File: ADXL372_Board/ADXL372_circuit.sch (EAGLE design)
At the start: 38 parts, among them IC4 SI7006-A20-IM, IC5 LP5907MFX-2.5/NOPB, Q2 BSS138W, SW1 DHT-4235A, U1 MX25R1635FM1IL0, U2 ADXL345BCCZ, U3 ADXL372BCCZ-RL7, Y1 16MHZ_X053201602002, Y2 3.2768KHZ

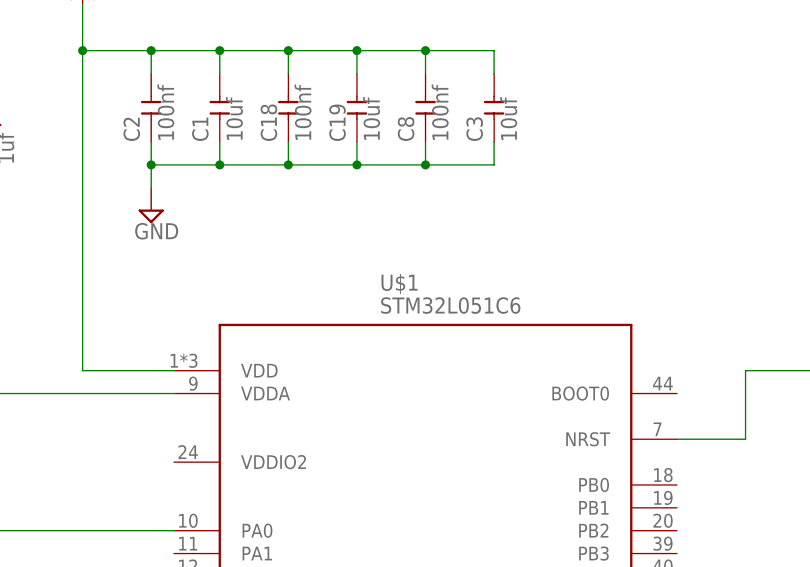
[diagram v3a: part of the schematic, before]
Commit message: パターン図を修正
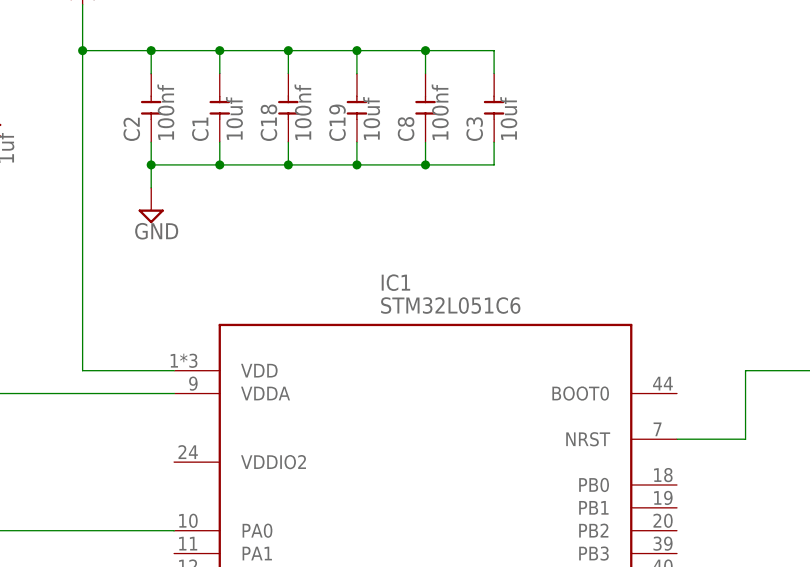
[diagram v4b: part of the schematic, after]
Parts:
- renumbered U$1 to IC1
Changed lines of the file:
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@@
 <part name="SUPPLY21" library="supply2" library_urn="urn:adsk.eagle:library:372" deviceset="GND" device=""/>
 <part name="Y1" library="OPL_Crystal Oscillator" library_urn="urn:adsk.eagle:library:8004402" deviceset="SMD-CRYSTAL-16MHZ-8PF-20PPM-40R(2P-5.0X3.2MM)" device="" package3d_urn="urn:adsk.eagle:package:8004459/1" value="16MHZ_X053201602002"/>
-<part name="U$1" library="stm32l05x6" library_urn="urn:adsk.eagle:library:14260580" deviceset="STM32L051C6" device="" package3d_urn="urn:adsk.eagle:package:19290/2"/>
+<part name="IC1" library="stm32l05x6" library_urn="urn:adsk.eagle:library:14260580" deviceset="STM32L051C6" device="" package3d_urn="urn:adsk.eagle:package:19290/2"/>
 <part name="C18" library="OPL_Capacitor" deviceset="CERAMIC-100NF-50V-10%-X7R(0603)" device="" package3d_urn="urn:adsk.eagle:package:8004287/1" value="100nf"/>
 <part name="C19" library="OPL_Capacitor" deviceset="CERAMIC-10UF-10V-(-20%～+80%)-Y5V(0805)" device="" package3d_urn="urn:adsk.eagle:package:8004286/1" value="10uf"/>
@@
 <attribute name="VALUE" x="138.43" y="96.52" size="1.27" layer="96" ratio="10"/>
 </instance>
-<instance part="U$1" gate="G$1" x="185.42" y="142.24" smashed="yes">
+<instance part="IC1" gate="G$1" x="185.42" y="142.24" smashed="yes">
 <attribute name="NAME" x="180.34" y="186.69" size="1.778" layer="95"/>
 <attribute name="VALUE" x="180.34" y="184.15" size="1.778" layer="96"/>
@@
 <wire x1="177.8" y1="210.82" x2="177.8" y2="213.36" width="0.1524" layer="91"/>
 <junction x="177.8" y="213.36"/>
-<pinref part="U$1" gate="G$1" pin="VDD"/>
+<pinref part="IC1" gate="G$1" pin="VDD"/>
 <wire x1="157.48" y1="177.8" x2="147.32" y2="177.8" width="0.1524" layer="91"/>
 </segment>
@@
 <pinref part="C12" gate="G$1" pin="2"/>
 <pinref part="VCC2" gate="G$1" pin="+3V3"/>
-<pinref part="U$1" gate="G$1" pin="VDDA"/>
+<pinref part="IC1" gate="G$1" pin="VDDA"/>
 <wire x1="157.48" y1="175.26" x2="121.92" y2="175.26" width="0.1524" layer="91"/>
 </segment>
@@
 <pinref part="SUPPLY2" gate="GND" pin="GND"/>
 <wire x1="218.44" y1="101.6" x2="218.44" y2="95.25" width="0.1524" layer="91"/>
-<pinref part="U$1" gate="G$1" pin="VSS"/>
+<pinref part="IC1" gate="G$1" pin="VSS"/>
 <wire x1="213.36" y1="101.6" x2="218.44" y2="101.6" width="0.1524" layer="91"/>
 </segment>
@@
 <wire x1="144.78" y1="109.22" x2="139.7" y2="109.22" width="0.1524" layer="91"/>
 <wire x1="144.78" y1="107.95" x2="144.78" y2="109.22" width="0.1524" layer="91"/>
-<pinref part="U$1" gate="G$1" pin="PC14-OSC32_IN"/>
+<pinref part="IC1" gate="G$1" pin="PC14-OSC32_IN"/>
 <wire x1="157.48" y1="109.22" x2="144.78" y2="109.22" width="0.1524" layer="91"/>
 <junction x="144.78" y="109.22"/>
@@
 <wire x1="144.78" y1="99.06" x2="144.78" y2="100.33" width="0.1524" layer="91"/>
 <junction x="144.78" y="99.06"/>
-<pinref part="U$1" gate="G$1" pin="PC15-OSC32_OUT"/>
+<pinref part="IC1" gate="G$1" pin="PC15-OSC32_OUT"/>
 <wire x1="157.48" y1="104.14" x2="149.86" y2="104.14" width="0.1524" layer="91"/>
 </segment>
@@
 <wire x1="243.84" y1="175.26" x2="243.84" y2="177.8" width="0.1524" layer="91"/>
 <junction x="243.84" y="177.8"/>
-<pinref part="U$1" gate="G$1" pin="NRST"/>
+<pinref part="IC1" gate="G$1" pin="NRST"/>
 <wire x1="213.36" y1="170.18" x2="220.98" y2="170.18" width="0.1524" layer="91"/>
 <wire x1="220.98" y1="170.18" x2="220.98" y2="177.8" width="0.1524" layer="91"/>
@@
 <label x="55.88" y="33.02" size="1.778" layer="95"/>
 <label x="193.04" y="45.72" size="1.778" layer="95"/>
-<pinref part="U$1" gate="G$1" pin="PA5"/>
+<pinref part="IC1" gate="G$1" pin="PA5"/>
 </segment>
 <segment>
@@
 <label x="193.04" y="38.1" size="1.778" layer="95"/>
 <label x="144.78" y="45.72" size="1.778" layer="95"/>
-<pinref part="U$1" gate="G$1" pin="PA6"/>
+<pinref part="IC1" gate="G$1" pin="PA6"/>
 </segment>
 <segment>
@@
 <label x="193.04" y="40.64" size="1.778" layer="95"/>
 <label x="144.78" y="50.8" size="1.778" layer="95"/>
-<pinref part="U$1" gate="G$1" pin="PA7"/>
+<pinref part="IC1" gate="G$1" pin="PA7"/>
 </segment>
 <segment>
@@
 <label x="132.08" y="139.7" size="1.778" layer="95"/>
 <label x="55.88" y="38.1" size="1.778" layer="95"/>
-<pinref part="U$1" gate="G$1" pin="PA8"/>
+<pinref part="IC1" gate="G$1" pin="PA8"/>
 </segment>
 </net>
@@
 <label x="132.08" y="137.16" size="1.778" layer="95"/>
 <label x="193.04" y="43.18" size="1.778" layer="95"/>
-<pinref part="U$1" gate="G$1" pin="PA9"/>
+<pinref part="IC1" gate="G$1" pin="PA9"/>
 </segment>
 </net>
@@
 <wire x1="157.48" y1="134.62" x2="129.54" y2="134.62" width="0.1524" layer="91"/>
 <label x="132.08" y="134.62" size="1.778" layer="95"/>
-<pinref part="U$1" gate="G$1" pin="PA10"/>
+<pinref part="IC1" gate="G$1" pin="PA10"/>
 </segment>
 </net>
@@
 <net name="I2C1_SCL" class="0">
 <segment>
-<pinref part="U$1" gate="G$1" pin="PB8"/>
+<pinref part="IC1" gate="G$1" pin="PB8"/>
 <wire x1="213.36" y1="144.78" x2="238.76" y2="144.78" width="0.1524" layer="91"/>
 <label x="220.98" y="144.78" size="1.778" layer="95"/>
@@
 <net name="I2C1_SDA" class="0">
 <segment>
-<pinref part="U$1" gate="G$1" pin="PB9"/>
+<pinref part="IC1" gate="G$1" pin="PB9"/>
 <wire x1="213.36" y1="142.24" x2="238.76" y2="142.24" width="0.1524" layer="91"/>
 <label x="220.98" y="142.24" size="1.778" layer="95"/>
@@
 <net name="I2C2_SCL" class="0">
 <segment>
-<pinref part="U$1" gate="G$1" pin="PB13"/>
+<pinref part="IC1" gate="G$1" pin="PB13"/>
 <wire x1="213.36" y1="132.08" x2="238.76" y2="132.08" width="0.1524" layer="91"/>
 <label x="220.98" y="132.08" size="1.778" layer="95"/>
@@
 <net name="I2C2_SDA" class="0">
 <segment>
-<pinref part="U$1" gate="G$1" pin="PB14"/>
+<pinref part="IC1" gate="G$1" pin="PB14"/>
 <wire x1="213.36" y1="129.54" x2="238.76" y2="129.54" width="0.1524" layer="91"/>
 <label x="220.98" y="129.54" size="1.778" layer="95"/>
@@
 <net name="N$14" class="0">
 <segment>
-<pinref part="U$1" gate="G$1" pin="PH0-OSC_IN"/>
+<pinref part="IC1" gate="G$1" pin="PH0-OSC_IN"/>
 <wire x1="213.36" y1="119.38" x2="233.68" y2="119.38" width="0.1524" layer="91"/>
 <pinref part="Y2" gate="G$1" pin="2"/>
@@
 <net name="N$15" class="0">
 <segment>
-<pinref part="U$1" gate="G$1" pin="PH1-OSC_OUT"/>
+<pinref part="IC1" gate="G$1" pin="PH1-OSC_OUT"/>
 <wire x1="213.36" y1="114.3" x2="223.52" y2="114.3" width="0.1524" layer="91"/>
 <wire x1="223.52" y1="114.3" x2="223.52" y2="106.68" width="0.1524" layer="91"/>
@@
 <net name="N$17" class="0">
 <segment>
-<pinref part="U$1" gate="G$1" pin="PA0"/>
+<pinref part="IC1" gate="G$1" pin="PA0"/>
 <wire x1="157.48" y1="160.02" x2="114.3" y2="160.02" width="0.1524" layer="91"/>
 <wire x1="114.3" y1="160.02" x2="114.3" y2="139.7" width="0.1524" layer="91"/>

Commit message: 回路図修正
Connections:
- removed net N$16: IC1.PA10
- removed net N$24: U1.CS#
- removed net N$5: U3.SCLK
- removed net N$6: U3.!CS!/SCL
- removed net N$7: U3.MOSI/SDA
- removed net N$8: U3.MISO
- new net FLASH_MEMORY: IC1.PA10, U1.CS#
- net ADXL372_CS: now also U3.!CS!/SCL
- net SPI1_MISO: now also U3.MISO
- net SPI1_MOSI: now also U3.MOSI/SDA
- net SPI1_SCK: now also U3.SCLK
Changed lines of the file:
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@@
 <part name="BT1" library="BU2032SM-HD-G" library_urn="urn:adsk.eagle:library:14268586" deviceset="BU2032SM-HD-G" device="" package3d_urn="urn:adsk.eagle:package:14268589/1"/>
 <part name="VCC1" library="supply1" library_urn="urn:adsk.eagle:library:371" deviceset="+3V3" device="" value="+2V5"/>
-<part name="VCC2" library="supply1" library_urn="urn:adsk.eagle:library:371" deviceset="+3V3" device="" value="+2V5"/>
+<part name="VCC" library="supply1" library_urn="urn:adsk.eagle:library:371" deviceset="+3V3" device="" value="+2V5"/>
 <part name="VCC3" library="supply1" library_urn="urn:adsk.eagle:library:371" deviceset="+3V3" device="" value="+2V5"/>
 <part name="VCC4" library="supply1" library_urn="urn:adsk.eagle:library:371" deviceset="+3V3" device="" value="+2V5"/>
@@
 <attribute name="VALUE" x="144.78" y="222.25" size="1.778" layer="96"/>
 </instance>
-<instance part="VCC2" gate="G$1" x="121.92" y="218.44" smashed="yes">
+<instance part="VCC" gate="G$1" x="121.92" y="218.44" smashed="yes">
 <attribute name="VALUE" x="119.38" y="219.71" size="1.778" layer="96"/>
 </instance>
@@
 <pinref part="C11" gate="G$1" pin="2"/>
 <pinref part="C12" gate="G$1" pin="2"/>
-<pinref part="VCC2" gate="G$1" pin="+3V3"/>
+<pinref part="VCC" gate="G$1" pin="+3V3"/>
 <pinref part="IC1" gate="G$1" pin="VDDA"/>
 <wire x1="157.48" y1="175.26" x2="121.92" y2="175.26" width="0.1524" layer="91"/>
@@
 <label x="132.08" y="147.32" size="1.778" layer="95"/>
 <label x="55.88" y="33.02" size="1.778" layer="95"/>
-<label x="193.04" y="45.72" size="1.778" layer="95"/>
 <pinref part="IC1" gate="G$1" pin="PA5"/>
 </segment>
@@
 <label x="289.56" y="119.38" size="1.778" layer="95"/>
 </segment>
+<segment>
+<pinref part="U3" gate="G$1" pin="SCLK"/>
+<wire x1="210.82" y1="45.72" x2="190.5" y2="45.72" width="0.1524" layer="91"/>
+<label x="193.04" y="45.72" size="1.778" layer="95"/>
+</segment>
 </net>
 <net name="SPI1_MISO" class="0">
@@
 <wire x1="157.48" y1="144.78" x2="129.54" y2="144.78" width="0.1524" layer="91"/>
 <label x="132.08" y="144.78" size="1.778" layer="95"/>
-<label x="193.04" y="38.1" size="1.778" layer="95"/>
-<label x="193.04" y="38.1" size="1.778" layer="95"/>
 <label x="144.78" y="45.72" size="1.778" layer="95"/>
 <pinref part="IC1" gate="G$1" pin="PA6"/>
@@
 <label x="289.56" y="114.3" size="1.778" layer="95"/>
 </segment>
+<segment>
+<pinref part="U3" gate="G$1" pin="MISO"/>
+<wire x1="210.82" y1="38.1" x2="190.5" y2="38.1" width="0.1524" layer="91"/>
+<label x="193.04" y="38.1" size="1.778" layer="95"/>
+</segment>
 </net>
 <net name="SPI1_MOSI" class="0">
@@
 <wire x1="157.48" y1="142.24" x2="129.54" y2="142.24" width="0.1524" layer="91"/>
 <label x="132.08" y="142.24" size="1.778" layer="95"/>
-<label x="193.04" y="40.64" size="1.778" layer="95"/>
 <label x="144.78" y="50.8" size="1.778" layer="95"/>
 <pinref part="IC1" gate="G$1" pin="PA7"/>
@@
 <label x="289.56" y="116.84" size="1.778" layer="95"/>
 </segment>
+<segment>
+<pinref part="U3" gate="G$1" pin="MOSI/SDA"/>
+<wire x1="210.82" y1="40.64" x2="190.5" y2="40.64" width="0.1524" layer="91"/>
+<label x="193.04" y="40.64" size="1.778" layer="95"/>
+</segment>
 </net>
 <net name="N$4" class="0">
@@
 <pinref part="U2" gate="A" pin="SCL/SCLK"/>
 <wire x1="53.34" y1="33.02" x2="76.2" y2="33.02" width="0.1524" layer="91"/>
-</segment>
-</net>
-<net name="N$5" class="0">
-<segment>
-<pinref part="U3" gate="G$1" pin="SCLK"/>
-<wire x1="210.82" y1="45.72" x2="190.5" y2="45.72" width="0.1524" layer="91"/>
-</segment>
-</net>
-<net name="N$6" class="0">
-<segment>
-<pinref part="U3" gate="G$1" pin="!CS!/SCL"/>
-<wire x1="210.82" y1="43.18" x2="190.5" y2="43.18" width="0.1524" layer="91"/>
-</segment>
-</net>
-<net name="N$7" class="0">
-<segment>
-<pinref part="U3" gate="G$1" pin="MOSI/SDA"/>
-<wire x1="210.82" y1="40.64" x2="190.5" y2="40.64" width="0.1524" layer="91"/>
-</segment>
-</net>
-<net name="N$8" class="0">
-<segment>
-<pinref part="U3" gate="G$1" pin="MISO"/>
-<wire x1="210.82" y1="38.1" x2="190.5" y2="38.1" width="0.1524" layer="91"/>
 </segment>
 </net>
@@
 <wire x1="157.48" y1="137.16" x2="129.54" y2="137.16" width="0.1524" layer="91"/>
 <label x="132.08" y="137.16" size="1.778" layer="95"/>
+<pinref part="IC1" gate="G$1" pin="PA9"/>
+</segment>
+<segment>
+<pinref part="U3" gate="G$1" pin="!CS!/SCL"/>
+<wire x1="210.82" y1="43.18" x2="190.5" y2="43.18" width="0.1524" layer="91"/>
 <label x="193.04" y="43.18" size="1.778" layer="95"/>
-<pinref part="IC1" gate="G$1" pin="PA9"/>
-</segment>
-</net>
-<net name="N$16" class="0">
-<segment>
-<wire x1="157.48" y1="134.62" x2="129.54" y2="134.62" width="0.1524" layer="91"/>
-<label x="132.08" y="134.62" size="1.778" layer="95"/>
-<pinref part="IC1" gate="G$1" pin="PA10"/>
 </segment>
 </net>
@@
 </segment>
 </net>
-<net name="N$24" class="0">
+<net name="FLASH_MEMORY" class="0">
 <segment>
 <pinref part="U1" gate="G$1" pin="CS#"/>
 <wire x1="309.88" y1="121.92" x2="287.02" y2="121.92" width="0.1524" layer="91"/>
+<label x="289.56" y="121.92" size="1.778" layer="95"/>
+</segment>
+<segment>
+<wire x1="157.48" y1="134.62" x2="129.54" y2="134.62" width="0.1524" layer="91"/>
+<label x="132.08" y="134.62" size="1.778" layer="95"/>
+<pinref part="IC1" gate="G$1" pin="PA10"/>
 </segment>
 </net>
@@
 </segment>
 </net>
-<net name="VCC" class="0">
-<segment>
-<pinref part="+2V5" gate="VCC" pin="VCC"/>
-<pinref part="C15" gate="G$1" pin="2"/>
-<wire x1="93.98" y1="238.76" x2="93.98" y2="233.68" width="0.1524" layer="91"/>
-<pinref part="IC5" gate="G$1" pin="OUT"/>
-<wire x1="93.98" y1="233.68" x2="93.98" y2="231.14" width="0.1524" layer="91"/>
-<wire x1="71.12" y1="233.68" x2="86.36" y2="233.68" width="0.1524" layer="91"/>
-<junction x="93.98" y="233.68"/>
-<pinref part="C7" gate="G$1" pin="2"/>
-<wire x1="86.36" y1="233.68" x2="93.98" y2="233.68" width="0.1524" layer="91"/>
-<wire x1="86.36" y1="231.14" x2="86.36" y2="233.68" width="0.1524" layer="91"/>
-<junction x="86.36" y="233.68"/>
-</segment>
-</net>
 <net name="N$17" class="0">
 <segment>
@@
 </segment>
 </net>
+<net name="VCC" class="0">
+<segment>
+<pinref part="C7" gate="G$1" pin="2"/>
+<wire x1="86.36" y1="231.14" x2="86.36" y2="233.68" width="0.1524" layer="91"/>
+<pinref part="IC5" gate="G$1" pin="OUT"/>
+<wire x1="71.12" y1="233.68" x2="86.36" y2="233.68" width="0.1524" layer="91"/>
+<wire x1="86.36" y1="233.68" x2="93.98" y2="233.68" width="0.1524" layer="91"/>
+<junction x="86.36" y="233.68"/>
+<pinref part="+2V5" gate="VCC" pin="VCC"/>
+<wire x1="93.98" y1="238.76" x2="93.98" y2="233.68" width="0.1524" layer="91"/>
+<pinref part="C15" gate="G$1" pin="2"/>
+<wire x1="93.98" y1="231.14" x2="93.98" y2="233.68" width="0.1524" layer="91"/>
+<junction x="93.98" y="233.68"/>
+</segment>
+</net>

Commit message: Update circuit
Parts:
- removed U1: MX25R1635FM1IL0, MX25R1635FM1IL0:MX25R1635FM1IL0
- removed U2: ADXL345BCCZ, ADXL345BCCZ:ADXL345BCCZ
- removed U3: ADXL372BCCZ-RL7, ADXL372BCCZ-RL7:ADXL372BCCZ-RL7
- added CN1: FH12-08S-1SH, con-hirose:FH12-08S-1SH
- added IC2: ADXL345BCCZ, ADXL345BCCZ:ADXL345BCCZ
- added IC3: ADXL372BCCZ-RL7, ADXL372BCCZ-RL7:ADXL372BCCZ-RL7
- added IC6: MX25R1635FM1IL0, MX25R1635FM1IL0:MX25R1635FM1IL0
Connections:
- removed net N$10: U2.SDA/SDI/SDIO
- removed net N$11: U2.SDO/ALT_ADDRESS
- removed net N$17: IC1.PA0, R5.2
- removed net N$20: Q2.G, R4.2, R5.1
- removed net N$9: U2.*CS
- new net SPI1_NSS: IC1.PA4
- new net SPI2_MISO: IC1.PB14, IC6.SO/SIO1
- new net SPI2_MOSI: IC1.PB15, IC6.SI/SIO0
- new net SPI2_NSS: IC1.PB12
- new net SPI2_SCK: IC1.PB13, IC6.SCLK
- new net USART1_CK: CN1-3.1, IC1.PA8
- new net USART1_RX: CN1-5.1, IC1.PA10
- new net USART1_TX: CN1-4.1, IC1.PA9
- net +2V5: now also C14.2, C6.2, IC3.VDDI/O, IC3.VS
- net +3V3: now also CN1-1.1, CN1-2.1, IC2.VDD_I/O, IC2.VS, IC6.VCC; no longer C14.2, C6.2, U1.VCC, U2.VDD_I/O, U2.VS, U3.VDDI/O, U3.VS
- net ADXL345_CS: now also IC1.PA2, IC2.*CS; no longer IC1.PA8
- net ADXL372_CS: now also IC1.PA3, IC3.!CS!/SCL; no longer IC1.PA9, U3.!CS!/SCL
- net FLASH_MEMORY: now also IC1.PB11, IC6.CS#; no longer IC1.PA10, U1.CS#
- net GND: now also CN1-7.1, CN1-8.1, IC2.GND, IC2.GND_2, IC2.GND_3, IC3.GND, IC6.GND; no longer U1.GND, U2.GND, U2.GND_2, U2.GND_3, U3.GND
- net I2C2_SCL: no longer IC1.PB13
- net I2C2_SDA: no longer IC1.PB14
- net N$12: now also IC3.INT1; no longer U3.INT1
- net N$13: now also IC3.INT2; no longer U3.INT2
- net N$22: now also IC5.EN
- net N$4: now also Q2.G, R4.2, R5.2; no longer U2.SCL/SCLK
- net SPI1_MISO: now also IC2.SDO/ALT_ADDRESS, IC3.MISO; no longer U1.SO/SIO1, U3.MISO
- net SPI1_MOSI: now also IC2.SDA/SDI/SDIO, IC3.MOSI/SDA; no longer U1.SI/SIO0, U3.MOSI/SDA
- net SPI1_SCK: now also IC2.SCL/SCLK, IC3.SCLK; no longer U1.SCLK, U3.SCLK
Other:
- moved on the sheet: C14, C16, C17, C4, C5, C6, D1, IC4, Q2, R1, R2, R3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

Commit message: update circuit
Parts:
- removed BT1: BU2032SM-HD-G, BU2032SM-HD-G:BU2032SM-HD-G
- removed C15, C7: 10uf, OPL_Capacitor:CERAMIC-10UF-10V-(-20%～+80%)-Y5V(0805)
- removed IC5: LP5907MFX-2.5/NOPB, LP5907MFX-2.5_NOPB:LP5907MFX-2.5/NOPB
- added BT2: BU2032SM-HD-G, BU2032SM-HD-G:BU2032SM-HD-G
- added C22, C24, C25: 10uf, OPL_Capacitor:CERAMIC-10UF-10V-(-20%～+80%)-Y5V(0805)
- added C23: 100nf, OPL_Capacitor:CERAMIC-100NF-50V-10%-X7R(0603)
- added IC7: 74AHC1G14DCK, 74xx-little-us:74AHC1G14DCK
- added IC8: LP5907MFX-2.5/NOPB, LP5907MFX-2.5_NOPB:LP5907MFX-2.5/NOPB
- added R6: 10K 1/10W, OPL_Resistor:SMD-RES-10K-5%-1/10W(0603)
- added SW2: B3U-1000P-2P-SMD, OPL_Switch:SMD-BUTTON(2P-3.0X2.5X1.2+0.4MM)-B3U-1000P-2P-SMD
- added SW3: JS202011SCQN, JS202011SCQN:JS202011SCQN
- added TP1, TP2, TP3, TP4, TP5, TP6, TP7, TP8: TPB1,27, testpad:TPB1,27
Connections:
- removed net N$12: IC3.INT1
- removed net N$13: IC3.INT2
- removed net N$22: BT1.+, IC5.EN, IC5.IN
- new net +BAT: BT2.+, SW3.1, SW3.4
- new net +VIN: IC8.EN, IC8.IN, SW3.2, SW3.5
- new net 345_INT1: IC1.PA1, IC2.INT1
- new net 345_INT2: IC1.PA2, IC2.INT2
- new net 372_INT1: IC1.PB1, IC3.INT1
- new net 372_INT2: IC1.PB2, IC3.INT2
- new net MODE_LED: IC1.PB3, R5.1
- new net MODE_SW: IC1.PB4, IC7A.O
- new net N$10: IC1.PB7, TP7.TP
- new net N$11: IC1.PB10, TP8.TP
- new net N$5: IC7A.I, R6.1, SW2.2
- new net N$6: IC1.PA3, TP3.TP
- new net N$7: IC1.PA15, TP4.TP
- new net N$8: IC1.PB5, TP5.TP
- new net N$9: IC1.PB6, TP6.TP
- new net SYS_SWCLK: IC1.PA14, TP2.TP
- new net SYS_SWDIO: IC1.PA13, TP1.TP
- new net USART1_CTS: CN1-5.1, IC1.PA11
- new net USART1_RTS: CN1-6.1, IC1.PA12
- net +2V5: now also C22.2
- net +3V3: now also C23.2, IC7P.VCC, R6.2, SW3.3, SW3.6; no longer CN1-2.1
- net ADXL345_CS: now also IC1.PA0; no longer IC1.PA2
- net ADXL372_CS: now also IC1.PB0; no longer IC1.PA3
- net GND: now also BT2.-, C22.1, C23.1, C24.1, C25.1, IC7P.GND, IC8.GND, SW2.1; no longer BT1.-, C15.1, C7.1, IC5.GND
- net USART1_CK: now also CN1-2.1; no longer CN1-3.1
- net USART1_RX: now also CN1-4.1; no longer CN1-5.1
- net USART1_TX: now also CN1-3.1; no longer CN1-4.1
- net VCC: now also C24.2, C25.2, IC8.OUT; no longer C15.2, C7.2, IC5.OUT

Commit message: Update board design
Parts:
- C24: value 10uf -> 100nf; device OPL_Capacitor:CERAMIC-10UF-10V-(-20%～+80%)-Y5V(0805) -> OPL_Capacitor:CERAMIC-100NF-50V-10%-X7R(0603)
- renumbered Q2 to TR2
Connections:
- net N$3 renamed RESET
- removed net I2C2_SCL: IC4.SCL, R2.1
- removed net I2C2_SDA: IC4.SDA, R3.1
- removed net VCC: C24.2, C25.2, IC8.OUT
- net +2V5: now also C16.2, C17.2, C23.2, C24.2, C25.2, C4.2, C5.2, IC2.VDD_I/O, IC2.VS, IC4.VDD, IC6.VCC, IC7P.VCC, IC8.OUT, R1.2, R2.2, R3.2, R6.2
- net +3V3: no longer C16.2, C17.2, C23.2, C4.2, C5.2, IC2.VDD_I/O, IC2.VS, IC4.VDD, IC6.VCC, IC7P.VCC, R1.2, R2.2, R3.2, R6.2
- net I2C1_SCL: now also IC4.SCL, R2.1
- net I2C1_SDA: now also IC4.SDA, R3.1
